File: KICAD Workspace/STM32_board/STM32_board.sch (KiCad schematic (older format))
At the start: 25 parts, among them J1 Power connector, J10 Low side connector, J2 High side connector, J3 Sensors connector, J4 LCD interface, J5 Low side connector, J6 3v3_out, J7 Joystick connector, J9 UART module, U1 CD4050BE, U2 LM7805_TO220, U3 LP2950-3.3_TO92

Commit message: Final version for printing (i hope)
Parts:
- added J11, J8: Output pins, Connector_PinSocket_2.54mm:PinSocket_1x03_P2.54mm_Vertical, symbol Connector:Conn_01x03_Male
- C1, C2, C3, C4: footprint Capacitor_THT:CP_Radial_D5.0mm_P2.50mm -> Capacitor_THT:CP_Radial_D8.0mm_P3.50mm
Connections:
- net 12V: now also J1.1 (Pin_1); no longer J1.2 (Pin_2)
- net 3V3: now also J6.1 (Pin_1); no longer J6.2 (Pin_2)
- net ADC_BATTERY: now also TB1.P1_20 (PC4); no longer TB1.P1_18 (PA6)
- net CURRENT_SENSOR: now also TB1.P1_18 (PA6); no longer TB1.P1_20 (PC4)
- net EXT_4: now also TB1.P2_47 (PC6), J11.2 (Pin_2); no longer TB1.P1_24 (PB2)
- net EXT_5: now also J8.1 (Pin_1)
- net EXT_6: now also J8.2 (Pin_2)
- net EXT_7: now also J8.3 (Pin_3)
- net GND: now also J1.2 (Pin_2), J6.2 (Pin_2), J11.1 (Pin_1); no longer J1.1 (Pin_1), J6.1 (Pin_1)
- net EXT_3: now reaches TB1.P2_45 (PC8)
- net EXT_3: now also J11.3 (Pin_3)
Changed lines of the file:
@@
 Wire Wire Line
 	10100 1100 9150 1100
+Text Label 9150 1100 0    50   ~ 0
+12V
 Text Label 9150 1000 0    50   ~ 0
-12V
-Text Label 9150 1100 0    50   ~ 0
 GND
 Text Label 8700 4250 0    50   ~ 0
@@
 F 0 "C1" H 9068 4496 50  0000 L CNN
 F 1 "CP" H 9068 4405 50  0000 L CNN
-F 2 "Capacitor_THT:CP_Radial_D5.0mm_P2.50mm" H 8988 4300 50  0001 C CNN
+F 2 "Capacitor_THT:CP_Radial_D8.0mm_P3.50mm" H 8988 4300 50  0001 C CNN
 F 3 "~" H 8950 4450 50  0001 C CNN
 	1    8950 4450
@@
 F 0 "C2" H 10165 4546 50  0000 L CNN
 F 1 "C" H 10165 4455 50  0000 L CNN
-F 2 "Capacitor_THT:CP_Radial_D5.0mm_P2.50mm" H 10088 4350 50  0001 C CNN
+F 2 "Capacitor_THT:CP_Radial_D8.0mm_P3.50mm" H 10088 4350 50  0001 C CNN
 F 3 "~" H 10050 4500 50  0001 C CNN
 	1    10050 4500
@@
 F 0 "C4" H 10165 5696 50  0000 L CNN
 F 1 "C4" H 10165 5605 50  0000 L CNN
-F 2 "Capacitor_THT:CP_Radial_D5.0mm_P2.50mm" H 10088 5500 50  0001 C CNN
+F 2 "Capacitor_THT:CP_Radial_D8.0mm_P3.50mm" H 10088 5500 50  0001 C CNN
 F 3 "~" H 10050 5650 50  0001 C CNN
 	1    10050 5650
@@
 Wire Wire Line
 	10150 2950 9750 2950
+Text Label 9750 2950 0    50   ~ 0
+3V3
 Text Label 9750 2850 0    50   ~ 0
-3V3
-Text Label 9750 2950 0    50   ~ 0
 GND
 Wire Wire Line
@@
 F 0 "C3" H 9165 5746 50  0000 L CNN
 F 1 "C3" H 9165 5655 50  0000 L CNN
-F 2 "Capacitor_THT:CP_Radial_D5.0mm_P2.50mm" H 9088 5550 50  0001 C CNN
+F 2 "Capacitor_THT:CP_Radial_D8.0mm_P3.50mm" H 9088 5550 50  0001 C CNN
 F 3 "~" H 9050 5700 50  0001 C CNN
 	1    9050 5700
@@
 Text Label 5000 6000 0    50   ~ 0
 EXT_2
-Wire Wire Line
-	1500 3700 750  3700
-Text Label 750  3700 0    50   ~ 0
-EXT_4
 Wire Wire Line
 	3100 4500 3750 4500
@@
 Wire Wire Line
 	1500 2600 700  2600
-Text Label 700  2600 0    39   ~ 0
+Text Label 750  5600 0    39   ~ 0
 ADC_BATTERY
 Wire Wire Line
 	1500 5600 750  5600
-Text Label 750  5600 0    50   ~ 0
+Text Label 700  2600 0    50   ~ 0
 CURRENT_SENSOR
 Wire Wire Line
@@
 Text Label 750  3500 0    50   ~ 0
 READ_BATTERY
+$Comp
+L Connector:Conn_01x03_Male J8
+U 1 1 5C8F395E
+P 6150 6550
+F 0 "J8" H 6123 6480 50  0000 R CNN
+F 1 "Output pins" H 6123 6571 50  0000 R CNN
+F 2 "Connector_PinSocket_2.54mm:PinSocket_1x03_P2.54mm_Vertical" H 6150 6550 50  0001 C CNN
+F 3 "~" H 6150 6550 50  0001 C CNN
+	1    6150 6550
+	-1   0    0    1
+$EndComp
+Wire Wire Line
+	5950 6450 5000 6450
+Wire Wire Line
+	5950 6550 5000 6550
+Wire Wire Line
+	5950 6650 5000 6650
+Text Label 5000 6650 0    50   ~ 0
+EXT_5
+Text Label 5000 6550 0    50   ~ 0
+EXT_6
+Text Label 5000 6450 0    50   ~ 0
+EXT_7
+$Comp
+L Connector:Conn_01x03_Male J11
+U 1 1 5C914D72
+P 5550 5600
+F 0 "J11" H 5523 5530 50  0000 R CNN
+F 1 "Output pins" H 5523 5621 50  0000 R CNN
+F 2 "Connector_PinSocket_2.54mm:PinSocket_1x03_P2.54mm_Vertical" H 5550 5600 50  0001 C CNN
+F 3 "~" H 5550 5600 50  0001 C CNN
+	1    5550 5600
+	-1   0    0    1
+$EndComp
+Wire Wire Line
+	5350 5500 5050 5500
+Wire Wire Line
+	5350 5600 5050 5600
+Wire Wire Line
+	5350 5700 5050 5700
+Text Label 5050 5700 0    50   ~ 0
+GND
+Wire Wire Line
+	1500 6000 750  6000
+Wire Wire Line
+	1500 5800 750  5800
+Text Label 750  5800 0    50   ~ 0
+EXT_4
+Text Label 750  6000 0    50   ~ 0
+EXT_3
+Text Label 5050 5500 0    50   ~ 0
+EXT_3
+Text Label 5050 5600 0    50   ~ 0
+EXT_4
 $EndSCHEMATC

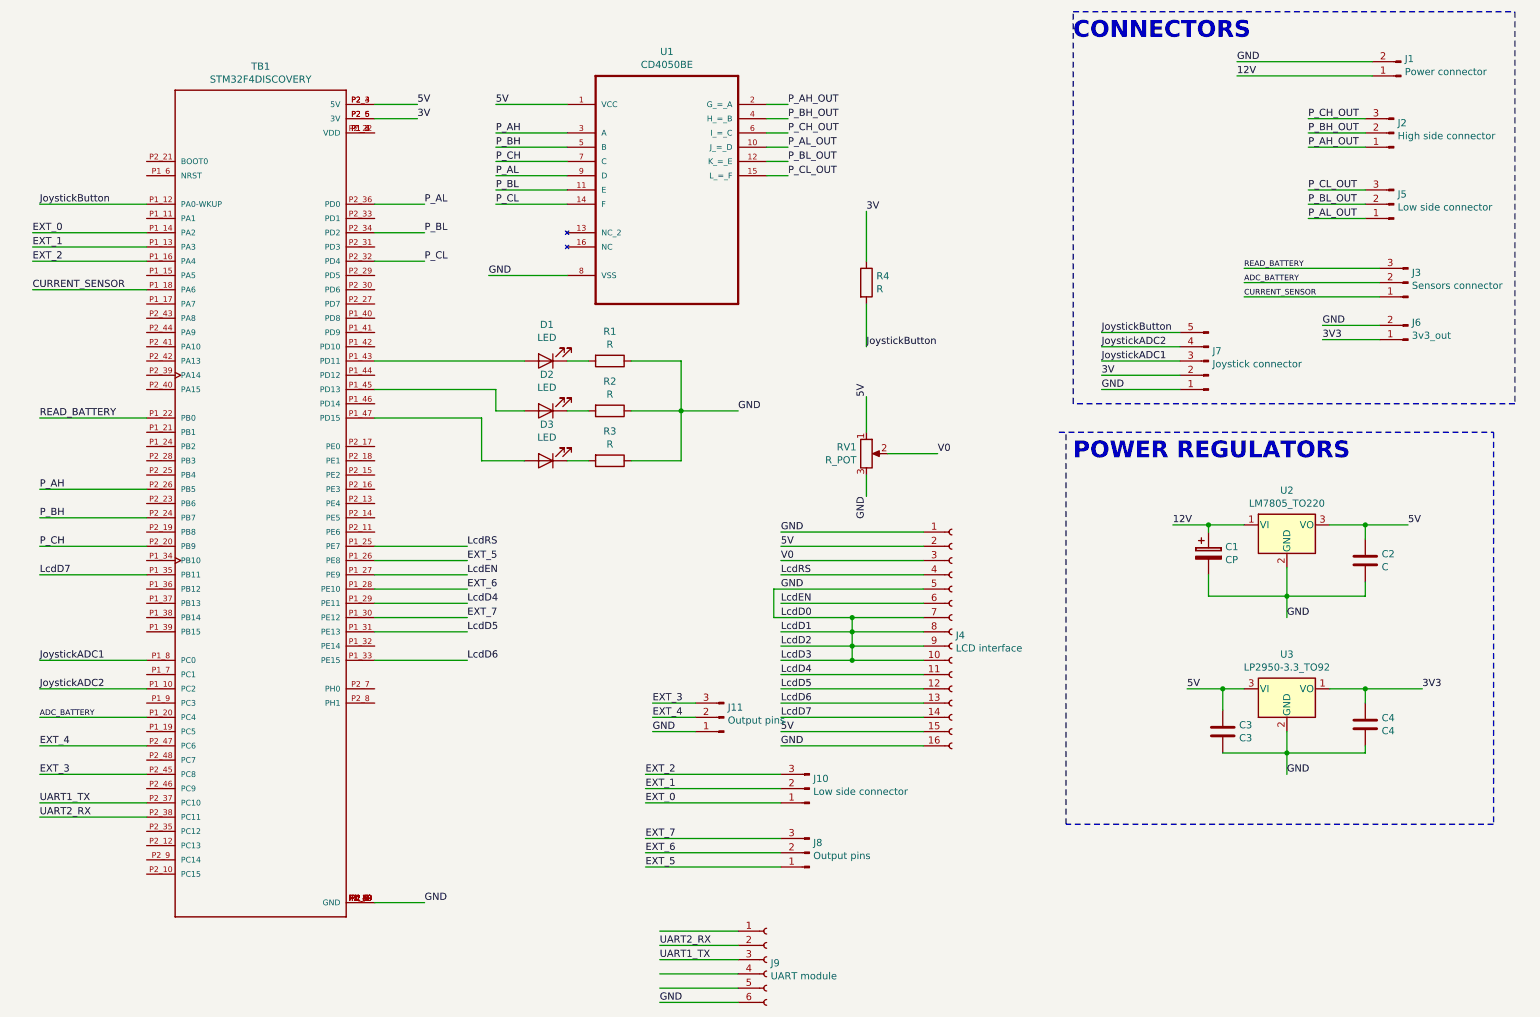
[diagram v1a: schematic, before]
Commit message: SMD version
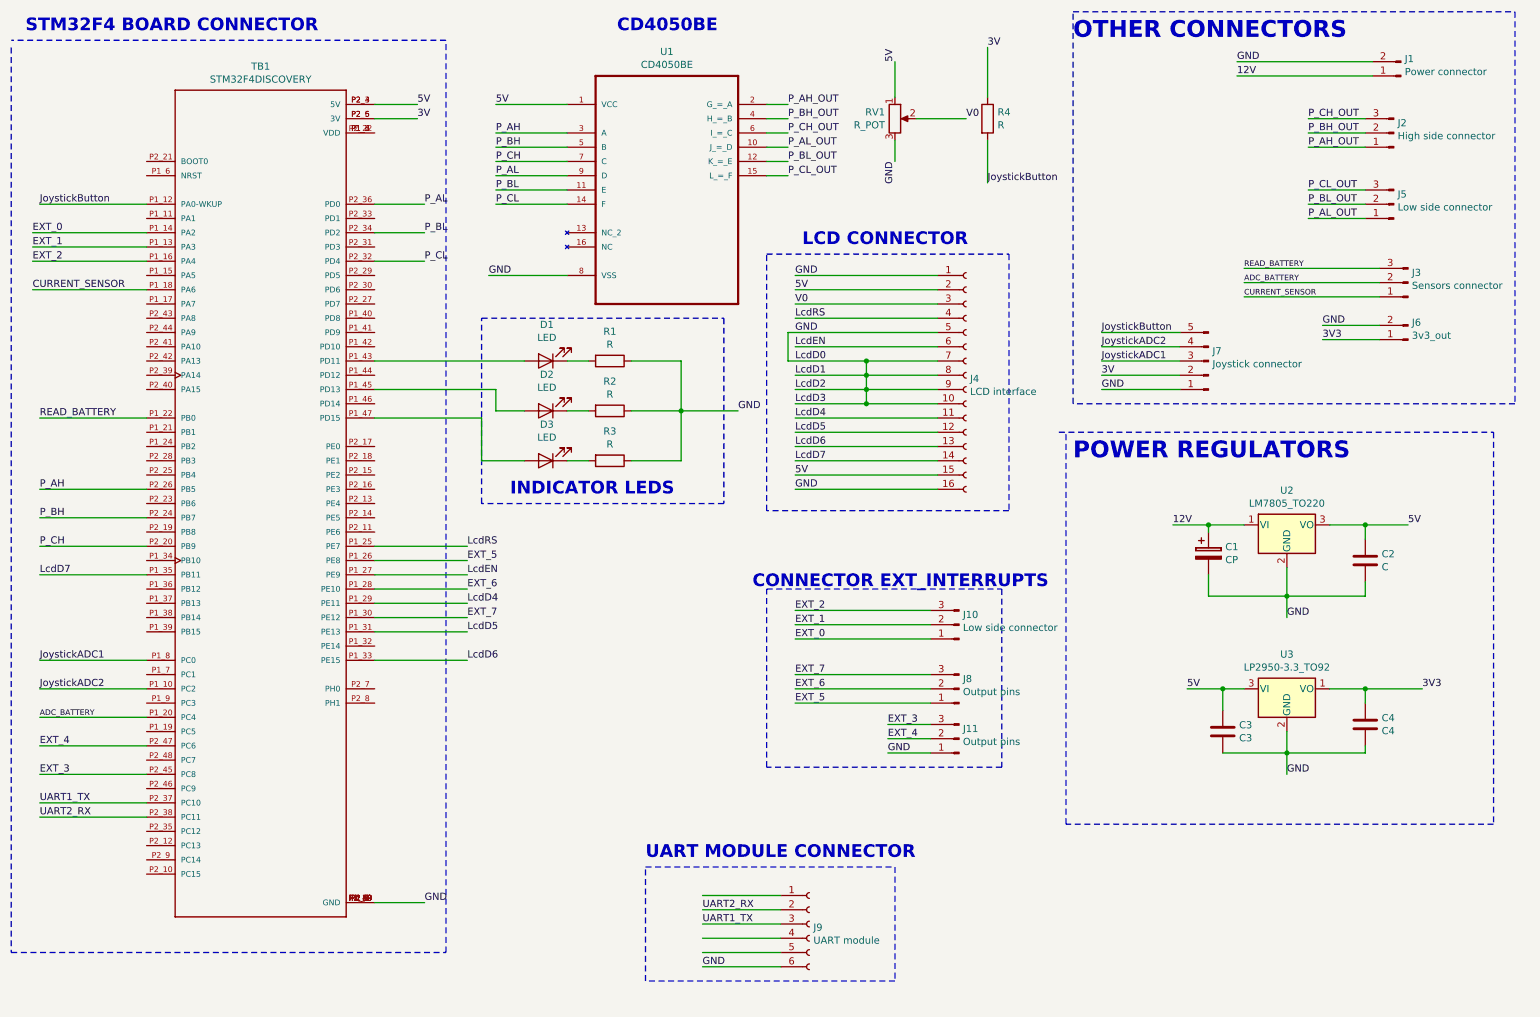
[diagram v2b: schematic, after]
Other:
- note added: "CD4050BE"
- note added: "CONNECTOR EXT_INTERRUPTS"
- note added: "INDICATOR LEDS\n"
- note added: "LCD CONNECTOR"
- note added: "OTHER CONNECTORS"
- note added: "STM32F4 BOARD CONNECTOR"
- note added: "UART MODULE CONNECTOR"
- note removed: "CONNECTORS"
- moved on the sheet: J10, J11, J4, J8, J9, R4, RV1
